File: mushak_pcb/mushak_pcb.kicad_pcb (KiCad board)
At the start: 2 copper layers, 45.8 x 53 mm, 112 parts, among them IC1 AS5600-ASOT, IC2 AS5600-ASOT, J1 Conn_01x04_Male, J10 IR_1, J11 AS5600_1, J12 IR_2, J13 AS5600_2, J14 IR_3, J15 ToF, J16 IR_4, J17 ToF, J2 Conn_01x02_Female, J3 BLE_Conn, J4 AS5600_Left, J5 AS5600_Right, J6 IR_1, J7 IR_3, J8 IR_2, J9 IR_4, M1 motor, M2 motor, Q1 DMN3065LW-7, Q2 DMN3065LW-7, Q3 DMN3065LW-7, Q4 DMN3065LW-7, Q5 DMN3065LW-7, SW1 SW_Push, SW2 SW_Push, U1 BA30BC0FP-E2, U3 DRV8833PW, U4 VL6180XV0NR/1, U5 MPU-6500, U6 STM32F405RGTx, Y1 25Mhz, Y2 32.769kHz

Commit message: completed routing
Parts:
- J2: footprint Connector_JST:JST_SHL_SM02B-SHLS-TF_1x02-1MP_P1.00mm_Horizontal -> Connector_JST:JST_EH_B2B-EH-A_1x02_P2.50mm_Vertical
- moved R23 362.7 mm to (291.7, -98.5)
- moved C35 361.4 mm to (288.8, -88.8)
- moved D5 361.4 mm to (262.6, -83.1)
- moved J6 361.4 mm to (280.5, -87.5)
- moved J8 361.4 mm to (280.5, -90.1)
- moved R7 361.4 mm to (278.5, -81.6)
- moved A1 361.4 mm to (263.0, -95.0)
- moved A2 361.4 mm to (275.8, -93.2)
- moved A3 361.4 mm to (263.0, -86.2)
- moved A4 361.4 mm to (263.0, -90.6)
- moved C34 361.4 mm to (280.9, -79.3)
- moved C36 361.4 mm to (284.6, -83.5)
- moved C37 361.4 mm to (283.6, -80.0)
- moved C38 361.4 mm to (295.3, -95.0)
- moved C39 361.4 mm to (281.9, -81.9)
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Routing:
- net +3V0: track 40.6 -> 195.1 mm, vias 0 -> 3
- net POW_GND: track 52.8 -> 120.9 mm, vias 10 -> 32
- net BUZZER_OP: track 0.00 -> 48.0 mm, vias 0 -> 4
- net BAT_VOL: track 1.58 -> 36.3 mm, vias 0 -> 2
- net /DRV8833_Motor_Driver/EN: track 0.00 -> 33.4 mm, vias 0 -> 2
- net POW_IN: track 19.5 -> 52.5 mm, vias 0 -> 3
- net /DRV8833_Motor_Driver/AIN2: track 0.00 -> 31.2 mm, vias 0 -> 2
- net NRST: track 2.07 -> 32.3 mm, vias 0 -> 2
- net SCL_3: track 0.00 -> 27.8 mm, vias 0 -> 2
- net SDA_3: track 0.00 -> 27.6 mm, vias 0 -> 2
- net /DRV8833_Motor_Driver/AIN1: track 0.00 -> 27.3 mm, vias 0 -> 2
- net DEBUG: track 2.18 -> 29.3 mm, vias 0 -> 2
- net IR_LED_4: track 0.00 -> 26.6 mm, vias 0 -> 2
- net /DRV8833_Motor_Driver/BIN2: track 0.00 -> 26.3 mm, vias 0 -> 2
- net /DRV8833_Motor_Driver/BIN1: track 0.00 -> 25.2 mm, vias 0 -> 2
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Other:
- outline, holes or cut-outs redrawn

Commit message: Completed sensor routing
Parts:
- C22, C23, C34, C35, C38, C39, D2, D3, D4, D5, R10, R11, R13, R22, R5, R6, R8, R9: moved to B.Cu
- moved J7 261.7 mm to (158.3, 128.3)
- moved C5 255.4 mm to (164.7, 126.4)
- moved R11 253.4 mm to (158.3, 126.5)
- moved Q2 252.9 mm to (164.2, 124.3), turned to 180 degrees
- moved C38 252.8 mm to (172.3, 125.8), turned to -90 degrees
- moved R6 252.7 mm to (164.7, 126.4)
- moved R23 252.6 mm to (172.4, 124.2), turned to 90 degrees
- moved C35 250.4 mm to (160.2, 126.0), turned to -90 degrees
- moved D3 248.2 mm to (158.7, 121.0), turned to -90 degrees
- moved J6 244.8 mm to (164.7, 128.2)
- moved J8 244.4 mm to (170.5, 128.2)
- moved R22 244.4 mm to (176.1, 126.5)
- moved A2 244.2 mm to (158.7, 121.0), turned to -90 degrees
- moved R13 243.9 mm to (170.6, 126.5)
- moved C6 243.5 mm to (158.3, 126.5)
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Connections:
- A1 pad 1: /IR_sensor/IR_REC -> /IR_sensor/IR_REC_1
- A1 pad 2: /IR_sensor/+3V0 -> /IR_sensor/+3V0_1
- A2 pad 1: /IR_sensor/IR_REC -> /IR_sensor/IR_REC_2
- A2 pad 2: /IR_sensor/+3V0 -> /IR_sensor/+3V0_2
- A3 pad 1: /IR_sensor/IR_REC -> /IR_sensor/IR_REC_4
- A3 pad 2: /IR_sensor/+3V0 -> /IR_sensor/+3V0_4
- A4 pad 1: /IR_sensor/IR_REC -> /IR_sensor/IR_REC_3
- A4 pad 2: /IR_sensor/+3V0 -> /IR_sensor/+3V0_3
- C34 pad 2: /IR_sensor/GND -> /IR_sensor/GND_1
- C35 pad 2: /IR_sensor/GND -> /IR_sensor/GND_2
- C36 pad 1: /IR_sensor/+3V0 -> /IR_sensor/+3V0_4
- C36 pad 2: /IR_sensor/GND -> /IR_sensor/GND_4
- C37 pad 1: /IR_sensor/+3V0 -> /IR_sensor/+3V0_3
- C37 pad 2: /IR_sensor/GND -> /IR_sensor/GND_3
- C38 pad 2: /IR_sensor/GND -> /IR_sensor/GND_4
- C39 pad 2: /IR_sensor/GND -> /IR_sensor/GND_3
- C5 pad 1: /IR_sensor/+3V0 -> /IR_sensor/+3V0_1
- C5 pad 2: /IR_sensor/GND -> /IR_sensor/GND_1
- C6 pad 1: /IR_sensor/+3V0 -> /IR_sensor/+3V0_2
- C6 pad 2: /IR_sensor/GND -> /IR_sensor/GND_2
- J6 pad 1: /IR_sensor/+3V0 -> /IR_sensor/+3V0_1
- J6 pad 2: /IR_sensor/IR_POW -> /IR_sensor/IR_POW_1
- J6 pad 3: /IR_sensor/IR_REC -> /IR_sensor/IR_REC_1
- J6 pad 4: /IR_sensor/GND -> /IR_sensor/GND_1
- J7 pad 1: /IR_sensor/+3V0 -> /IR_sensor/+3V0_2
- J7 pad 2: /IR_sensor/IR_POW -> /IR_sensor/IR_POW_2
- J7 pad 3: /IR_sensor/IR_REC -> /IR_sensor/IR_REC_2
- J7 pad 4: /IR_sensor/GND -> /IR_sensor/GND_2
- J8 pad 1: /IR_sensor/+3V0 -> /IR_sensor/+3V0_4
- J8 pad 2: /IR_sensor/IR_POW -> /IR_sensor/IR_POW_4
- J8 pad 3: /IR_sensor/IR_REC -> /IR_sensor/IR_REC_4
- J8 pad 4: /IR_sensor/GND -> /IR_sensor/GND_4
- J9 pad 1: /IR_sensor/+3V0 -> /IR_sensor/+3V0_3
- J9 pad 2: /IR_sensor/IR_POW -> /IR_sensor/IR_POW_3
- J9 pad 3: /IR_sensor/IR_REC -> /IR_sensor/IR_REC_3
- J9 pad 4: /IR_sensor/GND -> /IR_sensor/GND_3
- Q2 pad 2: /IR_sensor/IR_POW -> /IR_sensor/IR_POW_1
- Q2 pad 3: /IR_sensor/GND -> /IR_sensor/GND_1
- Q3 pad 2: /IR_sensor/IR_POW -> /IR_sensor/IR_POW_2
- Q3 pad 3: /IR_sensor/GND -> /IR_sensor/GND_2
- Q4 pad 2: /IR_sensor/IR_POW -> /IR_sensor/IR_POW_4
- Q4 pad 3: /IR_sensor/GND -> /IR_sensor/GND_4
- Q5 pad 2: /IR_sensor/IR_POW -> /IR_sensor/IR_POW_3
- Q5 pad 3: /IR_sensor/GND -> /IR_sensor/GND_3
- R11 pad 1: /IR_sensor/IR_REC -> /IR_sensor/IR_REC_2
- R11 pad 2: /IR_sensor/GND -> /IR_sensor/GND_2
- R12 pad 1: POW_IN -> /IR_sensor/+3V0_2
- R13 pad 1: /IR_sensor/IR_REC -> /IR_sensor/IR_REC_4
- R13 pad 2: /IR_sensor/GND -> /IR_sensor/GND_4
- R22 pad 1: /IR_sensor/IR_REC -> /IR_sensor/IR_REC_3
- R22 pad 2: /IR_sensor/GND -> /IR_sensor/GND_3
- R23 pad 1: POW_IN -> /IR_sensor/+3V0_4
- R24 pad 1: POW_IN -> /IR_sensor/+3V0_3
- R6 pad 1: /IR_sensor/IR_REC -> /IR_sensor/IR_REC_1
- R6 pad 2: /IR_sensor/GND -> /IR_sensor/GND_1
- R7 pad 1: POW_IN -> /IR_sensor/+3V0_1
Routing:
- net /AS5600_Right/+3V0_s: track 0.00 -> 14.8 mm, vias 0 -> 1
- net /AS5600_Left/+3V0_s: track 0.00 -> 14.6 mm, vias 0 -> 2
- net /IR_sensor/+3V0_1: track 0.00 -> 13.7 mm, vias 0 -> 1
- net /IR_sensor/+3V0_4: track 0.00 -> 13.4 mm, vias 0 -> 1
- net /IR_sensor/+3V0_3: track 0.00 -> 13.2 mm, vias 0 -> 1
- net /IR_sensor/+3V0_2: track 0.00 -> 13.2 mm, vias 0 -> 1
- net /AS5600_Right/GND_s: track 0.00 -> 12.0 mm, vias 0 -> 1
- net /AS5600_Left/GND_s: track 0.00 -> 11.3 mm, vias 0 -> 1
- net /IR_sensor/IR_REC_1: track 0.00 -> 10.3 mm, vias 0 -> 1
- net /IR_sensor/IR_REC_2: track 0.00 -> 10.3 mm, vias 0 -> 1
- net /IR_sensor/IR_REC_3: track 0.00 -> 10.2 mm, vias 0 -> 1
- net /IR_sensor/IR_REC_4: track 0.00 -> 10.2 mm, vias 0 -> 1
- net POW_GND: track 120.9 -> 112.2 mm, vias 32 -> 36
- net Net-(D5-Pad1): track 0.00 -> 7.22 mm, vias 0 -> 1
- net Net-(D4-Pad1): track 0.00 -> 7.08 mm, vias 0 -> 1
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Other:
- board size 45.8 x 53 mm -> 45.8 x 51.8 mm

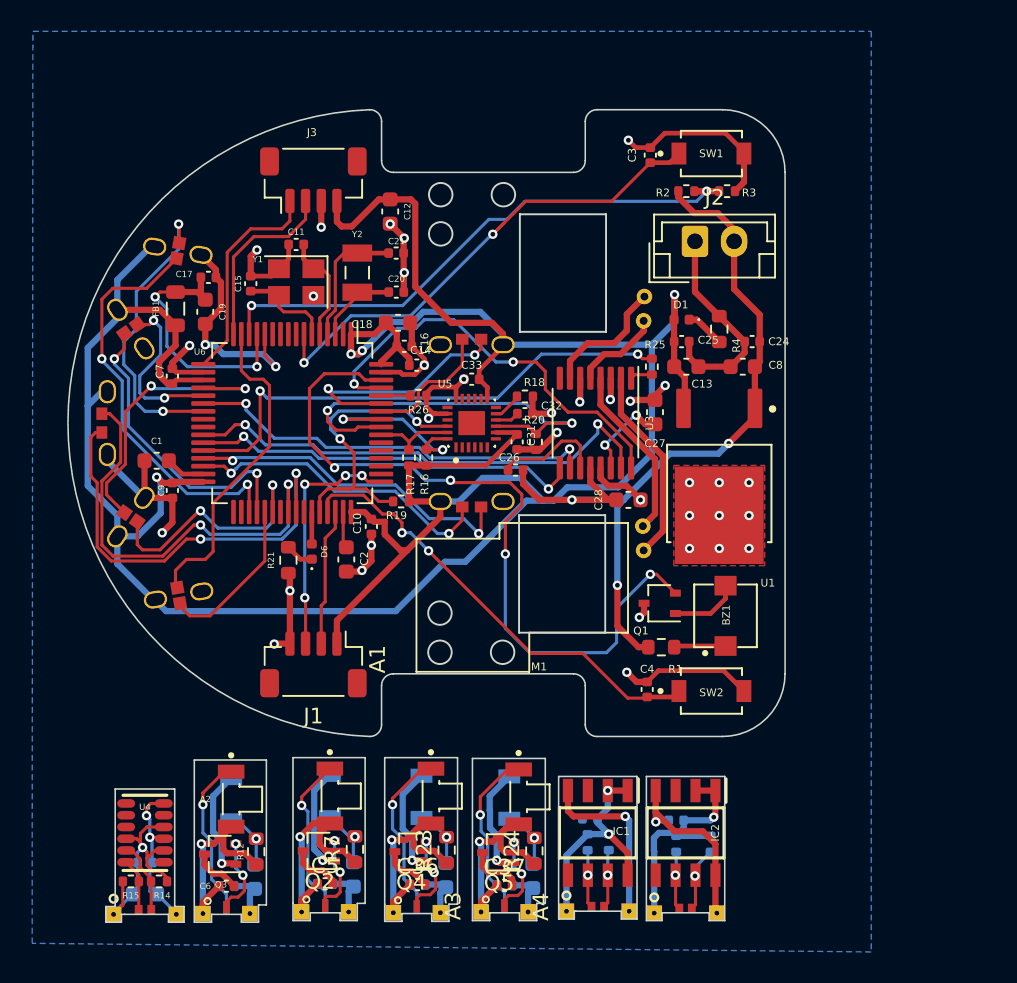
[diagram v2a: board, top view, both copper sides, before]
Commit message: modified pcb outline and graphics
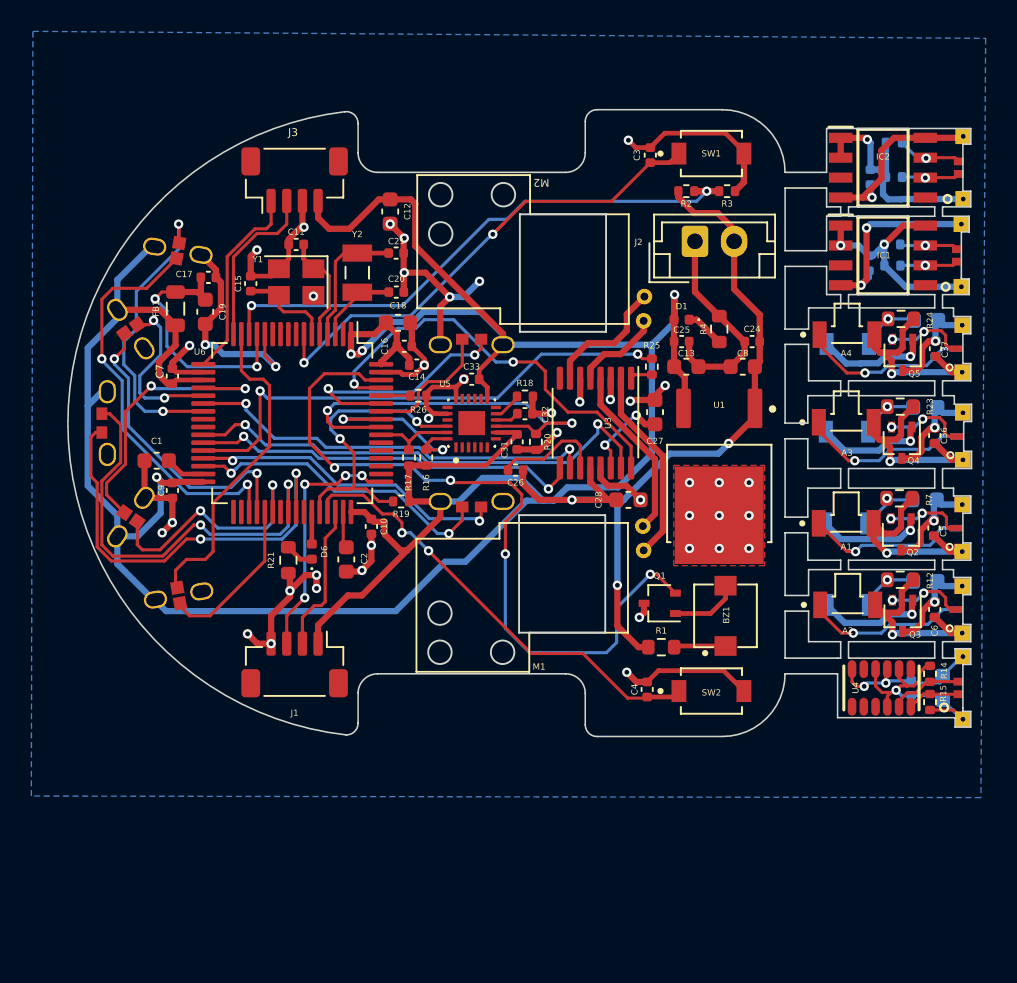
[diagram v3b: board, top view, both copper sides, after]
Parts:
- added G***: LOGO, mushak_mount_footprint:SRA_logo, B.Cu at (180.0, 97.0)
- added G***: LOGO, mushak_mount_footprint:mushak, B.Cu at (170.0, 97.0)
- moved J17 54.2 mm to (205.3, 113.9), turned to 90 degrees
- moved C29 52.6 mm to (204.1, 113.9), turned to 90 degrees
- moved R15 52.3 mm to (203.2, 114.8), turned to -90 degrees
- moved R14 51.0 mm to (203.2, 113.0), turned to 90 degrees
- moved J7 50.8 mm to (205.3, 108.9), turned to 90 degrees
- moved J5 50.8 mm to (205.4, 80.7), turned to 90 degrees
- moved C30 50.2 mm to (202.1, 113.9), turned to 90 degrees
- moved C6 48.5 mm to (203.6, 108.9), turned to 90 degrees
- moved R11 48.5 mm to (203.6, 108.9), turned to 90 degrees
- moved U4 47.9 mm to (200.2, 113.9), turned to 90 degrees
- moved J4 47.9 mm to (205.2, 86.3), turned to 90 degrees
- moved J6 47.5 mm to (205.3, 103.7), turned to 90 degrees
- moved C35 46.8 mm to (202.9, 107.1), turned to 0 degrees
- moved J9 46.3 mm to (205.3, 92.2), turned to 90 degrees
- moved R9 46.3 mm to (200.9, 79.1), turned to 0 degrees
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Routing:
- net POW_GND: track 112.2 -> 123.1 mm, vias 36 -> 42
- net TXD: track 13.9 -> 12.6 mm
- net /AS5600_Left/GND_s: track 11.3 -> 12.4 mm, vias 1 -> 2
- net SCL_2: track 21.5 -> 20.4 mm
- net RXD: track 11.7 -> 10.7 mm
- net SYS_JTMS-SWDIO: track 8.77 -> 9.53 mm
- net /IR_sensor/+3V0_2: track 13.2 -> 12.5 mm
- net +3V0: track 195.9 -> 196.5 mm
- net SYS_JTCK-SWCLK: track 15.5 -> 16.0 mm
- net /IR_sensor/GND_1: track 6.46 -> 6.26 mm, vias 0 -> 1
- net /IR_sensor/GND_2: track 6.21 -> 6.33 mm, vias 0 -> 1
- net /IR_sensor/GND_4: track 6.40 -> 6.32 mm, vias 0 -> 1
- net /IR_sensor/GND_3: vias 0 -> 1
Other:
- board size 45.8 x 51.8 mm -> 57.7 x 40 mm
- board text added: "Designed by - Chinmay Lonkar"
- board text added: "MUSHAK"

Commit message: modified graphics
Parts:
- removed the G*** at (170.0, 97.0)
- added G***: LOGO, mushak_mount_footprint:mooshak_small, F.Cu at (157.4, 111.4)
- added G***: LOGO, mushak_mount_footprint:mooshak, B.Cu at (163.2, 96.9)
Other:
- board text removed: "MUSHAK"
